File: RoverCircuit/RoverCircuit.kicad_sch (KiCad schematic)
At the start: 57 parts, among them J10 JST_5Pin_P2.54_H, J11_Sample_IR_Diode1 JST_2Pin_P2.54_V, J12_Satellite_IR_Diode1 JST_2Pin_P2.54_V, J13_Laser1 JST_2Pin_P2.54_V, J14_QRD_Board1 JST_5Pin_P2.54_V, J1_Servo1 JST_3Pin_P2.54_V, J2_Left_Wheel1 JST_4Pin_P2.54_V, J3_Right_Wheel1 JST_4Pin_P2.54_V, J4 JST_10Pin_P2.54_V, J5 JST_10Pin_P2.54_V, J6_Left_Sharp1 JST_3Pin_P2.54_V, J7_Right_Sharp1 JST_3Pin_P2.54_V, J8_Front_Sharp1 JST_3Pin_P2.54_V, J9_5v_Regulator1 JST_3Pin_P2.54_V, M1 Motor_Servo, M2 Left_Wheel, M3 Right_Wheel, Q1 PMOS, Q2 NMOS, Q3 QRD1114, Q4 QRD1114, Q5 QRD1114, Q6 NMOS, SW1 SW_SPST, U1 PIC24F16KA301, U2 LM1117T-3.3, U3 LM324

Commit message: Added low pass filters on every analog input
Used R=150, C=0.1uF to attenuate frequencies above the frequency of how fast the AD converter will read each signal.
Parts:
- removed SW1: SW_SPST, symbol Switch:SW_SPST
- added C10, C11, C12, C13, C14, C6, C7, C8, C9: 0.1uF, symbol Device:C
- added C3, C4, C5: 100uF, symbol Device:C_Polarized
- added J15_Ball_QRD1: JST_3Pin_P2.54_V, Connector_JST:JST_EH_B3B-EH-A_1x03_P2.50mm_Vertical, symbol Connector_Generic:Conn_01x03
- added Q7: QRD1114, Diode_THT:Diode_Bridge_DIP-4_W5.08mm_P2.54mm, symbol Custom_Symbol_Library:_1
- added R15: 10kΩ, Resistor_THT:R_Axial_DIN0207_L6.3mm_D2.5mm_P10.16mm_Horizontal, symbol Device:R
- added R16, R17, R18, R19, R20, R21, R22, R23, R24: 150Ω, symbol Device:R
- added R5: 330Ω, Resistor_THT:R_Axial_DIN0207_L6.3mm_D2.5mm_P10.16mm_Horizontal, symbol Device:R
- U1: footprint (none) -> Custom_Library:PIC_board
- U2: footprint Package_TO_SOT_THT:TO-220-3_Horizontal_TabDown -> Package_TO_SOT_THT:TO-220-3_Vertical
- renumbered J12_Satellite_IR_Diode1 to J12_Sat_Diode1
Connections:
- net 12v_Rail: now also Battery1.1 (Pin_1), C3.1
- net 3.3v_Rail: now also R15.2, R5.1
- net 5v_Rail: now also C4.1, C5.1; no longer J1_Servo1.1 (Pin_1), M1.1 (PWM)
- net Ball_Color_QRD_Input: now also C8.1, R18.2
- net Debug_LED_1: now also D1.2 (A)
- net Debug_LED_2: now also D2.2 (A)
- net Front_Sharp_Input: now also C14.1, R24.2; no longer J8_Front_Sharp1.1 (Pin_1), S3. (GND)
- net GND: now also C10.2, C11.2, C12.2, C13.2, C14.2, C3.2, C4.2, C5.2, C6.2, C7.2, C8.2, C9.2, J15_Ball_QRD1.1 (Pin_1), Q7.2 (GND), Q7.4 (GND)
- net Left_Of_Line_QRD_Input: now also C9.1, R19.2; no longer J10.5 (Pin_5), J14_QRD_Board1.5 (Pin_5), Q5.1 (Out), R11.1
- net Left_Sharp_Input: now also C12.1, R22.2; no longer J6_Left_Sharp1.1 (Pin_1), S1. (GND)
- net On_Line_QRD_Input: now also C10.1, R20.2; no longer J10.4 (Pin_4), J14_QRD_Board1.4 (Pin_4), Q4.1 (Out), R12.1
- net Right_Of_Line_QRD_Input: now also C11.1, R21.2; no longer J10.3 (Pin_3), J14_QRD_Board1.3 (Pin_3), Q3.1 (Out), R13.1
- net Right_Sharp_Input: now also C13.1, R23.2; no longer J7_Right_Sharp1.1 (Pin_1), S2. (GND)
- net Sample_Collection_IR_Input: now also C7.1, R17.2; no longer C1.2, R6.2, U3.1
- net Satellite_IR_Input: now also C6.1, R16.2; no longer C2.2, R7.2, U3.7
- net at Q1.1 (D), R1.1: now also J1_Servo1.1 (Pin_1), M1.1 (PWM)
- new net: J15_Ball_QRD1.3 (Pin_3), Q7.3 (Vin), R5.2
- new net Ball_Color_QRD_Output: J15_Ball_QRD1.2 (Pin_2), Q7.1 (Out), R15.1, R18.1
- new net Front_Sharp_Output: J8_Front_Sharp1.1 (Pin_1), R24.1, S3. (GND)
- new net Left_Of_Line_QRD_Output: J10.5 (Pin_5), J14_QRD_Board1.5 (Pin_5), Q5.1 (Out), R11.1, R19.1
- new net Left_Sharp_Output: J6_Left_Sharp1.1 (Pin_1), R22.1, S1. (GND)
- new net On_Line_QRD_Output: J10.4 (Pin_4), J14_QRD_Board1.4 (Pin_4), Q4.1 (Out), R12.1, R20.1
- new net Right_Of_Line_QRD_Output: J10.3 (Pin_3), J14_QRD_Board1.3 (Pin_3), Q3.1 (Out), R13.1, R21.1
- new net Right_Sharp_Output: J7_Right_Sharp1.1 (Pin_1), R23.1, S2. (GND)
- new net Sample_Collection_IR_Output: C1.2, R17.1, R6.2, U3.1
- new net Satellite_IR_Output: C2.2, R16.1, R7.2, U3.7
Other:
- note added: "Signal Conditioning"
- moved on the sheet: Battery1, J10, J13_Laser1, J14_QRD_Board1, J1_Servo1, J9_5v_Regulator1, LD1, M1, Q1, Q2, Q3, Q4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

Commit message: Updated title block
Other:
- company: (none) -> <INSERT NAME HERE> Rihard Bulloch, Kyle Chandler, Dane Baker, Spencer McHenry
- title: (none) -> ME 330: Mars Mini Rover
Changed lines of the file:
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@@
 	(generator_version "9.0")
 	(paper "A4")
+	(title_block
+		(title "ME 330: Mars Mini Rover")
+		(date "2026-10-26")
+		(company "<INSERT NAME HERE> Rihard Bulloch, Kyle Chandler, Dane Baker, Spencer McHenry")
+	)
 	(rectangle
 		(start 201.93 71.12)

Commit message: Added signal conditioning and reorganized the PCB
Also added bulk capacitors on each power rail
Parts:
- removed C5: 100uF, symbol Device:C_Polarized
- added C15: 100uF, Capacitor_THT:CP_Radial_D7.5mm_P2.50mm, symbol Device:C_Polarized
- C10, C11, C12, C13, C14, C6, C7, C8, C9: footprint (none) -> Capacitor_THT:C_Disc_D3.4mm_W2.1mm_P2.50mm
- C3, C4: footprint (none) -> Capacitor_THT:CP_Radial_D7.5mm_P2.50mm
- R16, R17, R18, R19, R20, R21, R22, R23, R24: footprint (none) -> Resistor_THT:R_Axial_DIN0207_L6.3mm_D2.5mm_P10.16mm_Horizontal
- R3, R4: value 330 -> 330Ω
- U1: footprint Custom_Library:PIC_board -> (none)
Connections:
- net 3.3v_Rail: now also C15.1
- net GND: now also C15.2
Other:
- moved on the sheet: U2

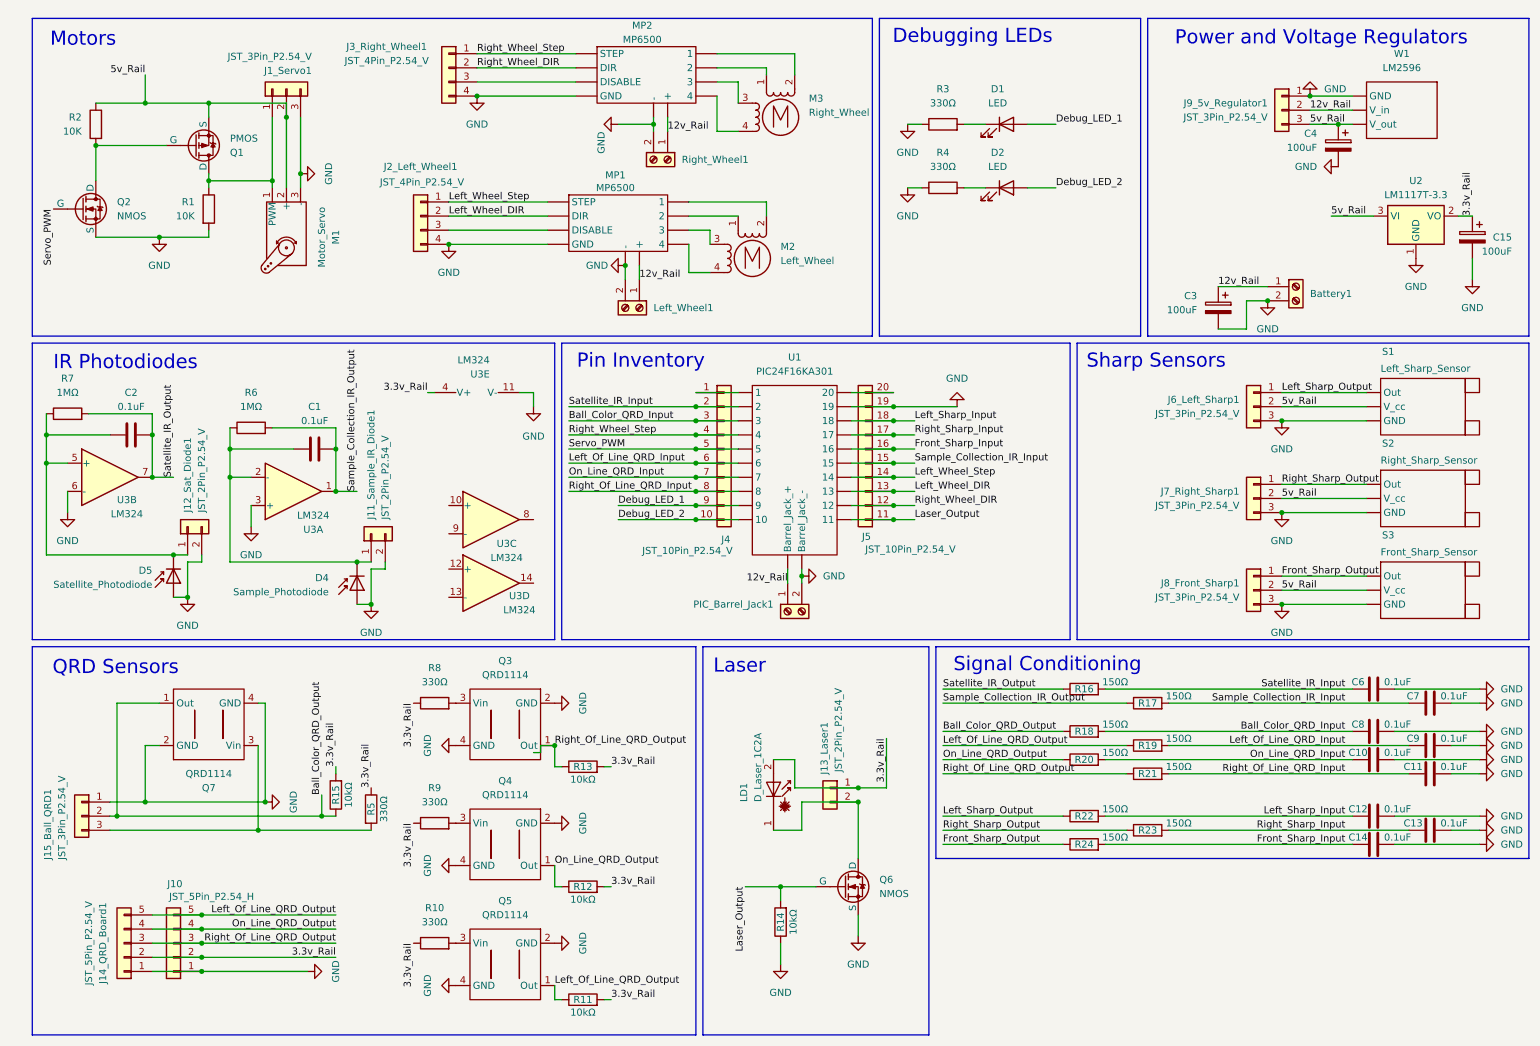
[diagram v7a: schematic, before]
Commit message: Finalized circuit diagram, functional line following
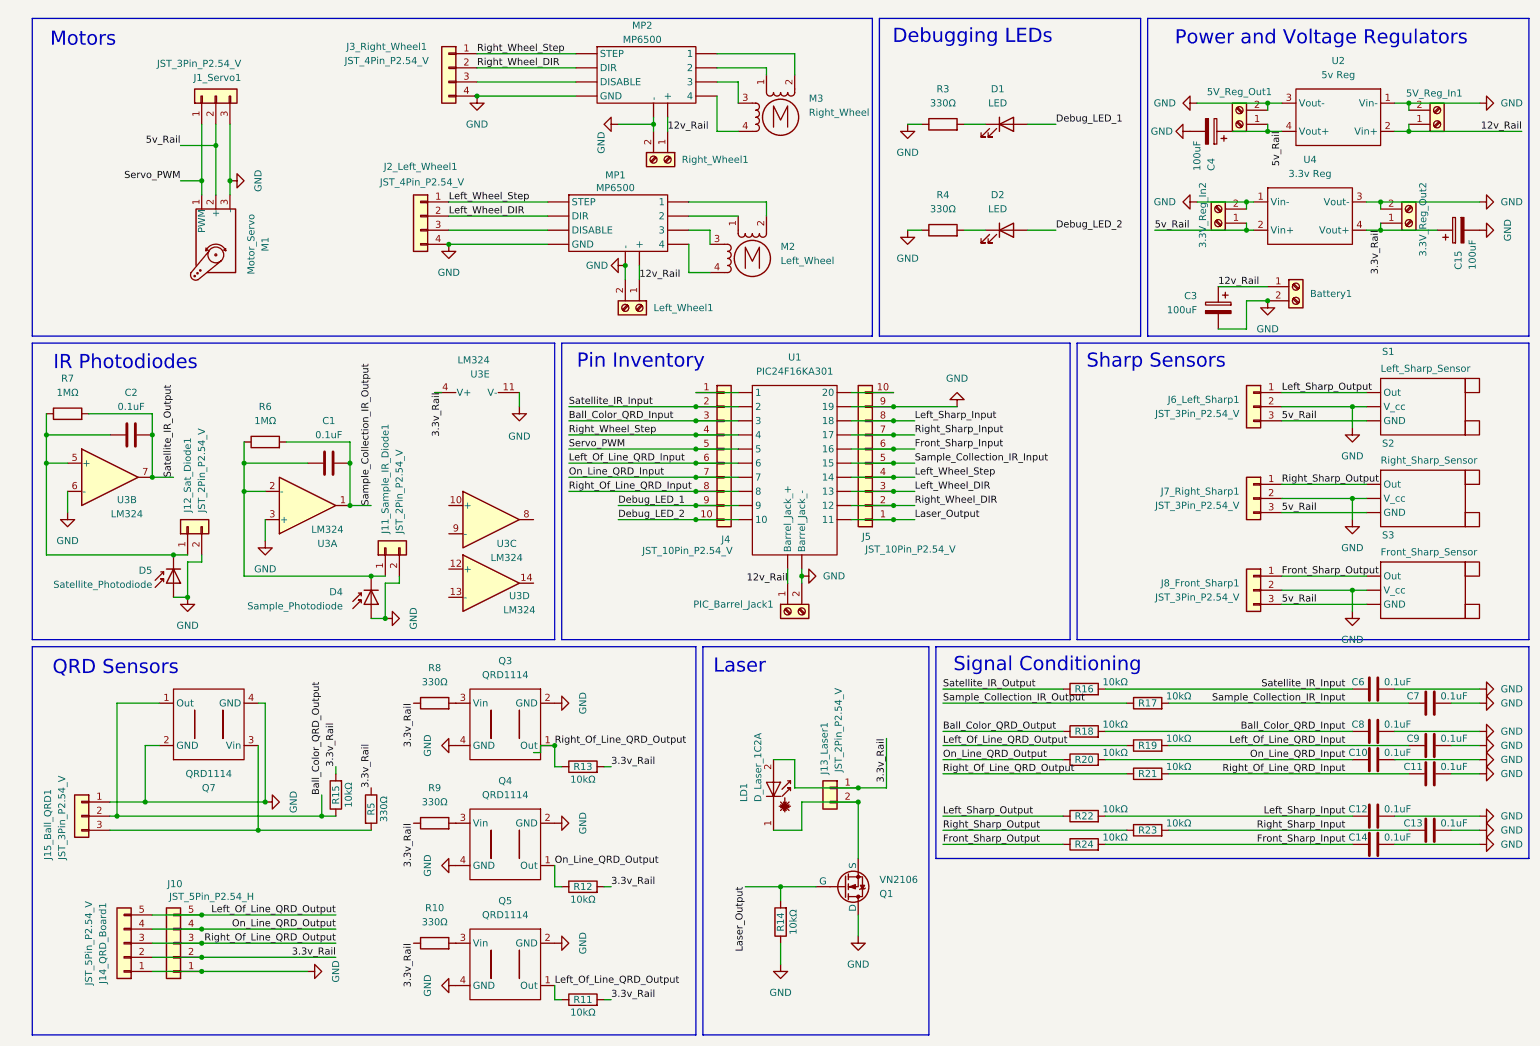
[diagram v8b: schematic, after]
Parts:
- removed J9_5v_Regulator1: JST_3Pin_P2.54_V, Connector_JST:JST_EH_B3B-EH-A_1x03_P2.50mm_Vertical, symbol Connector_Generic:Conn_01x03
- removed Q1: PMOS, Package_TO_SOT_THT:TO-92, symbol Simulation_SPICE:PMOS
- removed Q2: NMOS, Package_TO_SOT_THT:TO-92, symbol Simulation_SPICE:NMOS
- removed R1, R2: 10K, Resistor_THT:R_Axial_DIN0207_L6.3mm_D2.5mm_P10.16mm_Horizontal, symbol Device:R
- removed U2: LM1117T-3.3, Package_TO_SOT_THT:TO-220-3_Vertical, symbol Regulator_Linear:LM1117T-3.3
- removed W1: LM2596, symbol Custom_Symbol_Library:LM2596 - 5v Buck Converter
- added 3.3V_Reg_In2, 3.3V_Reg_Out2, 5V_Reg_In1, 5V_Reg_Out1: Battery_Terminal, Custom_Library:screw_terminal, symbol Connector:Screw_Terminal_01x02
- added U2: 5v Reg, symbol Custom_Symbol_Library:Variable_Voltage_Regulator
- added U4: 3.3v Reg, symbol Custom_Symbol_Library:Variable_Voltage_Regulator
- Q1: renamed from Q6; value NMOS -> VN2106; footprint Package_TO_SOT_THT:TO-92 -> Package_TO_SOT_THT:TO-92S
- R16, R17, R18, R19, R20, R21, R22, R23, R24: value 150Ω -> 10kΩ
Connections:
- net 12v_Rail: now also 5V_Reg_In1.1 (Pin_1), U2.2 (Vin+)
- net 3.3v_Rail: now also 3.3V_Reg_Out2.1 (Pin_1), U4.4 (Vout+)
- net 5v_Rail: now also J6_Left_Sharp1.3 (Pin_3), J7_Right_Sharp1.3 (Pin_3), J8_Front_Sharp1.3 (Pin_3), 3.3V_Reg_In2.1 (Pin_1), 5V_Reg_Out1.1 (Pin_1), U2.4 (Vout+), U4.2 (Vin+); no longer J6_Left_Sharp1.2 (Pin_2), J7_Right_Sharp1.2 (Pin_2), J8_Front_Sharp1.2 (Pin_2)
- net Front_Sharp_Input: now also J5.6 (Pin_6); no longer J5.16 (Pin_6)
- net GND: now also J5.9 (Pin_9), J6_Left_Sharp1.2 (Pin_2), J7_Right_Sharp1.2 (Pin_2), J8_Front_Sharp1.2 (Pin_2), Q1.1 (D), 3.3V_Reg_In2.2 (Pin_2), 3.3V_Reg_Out2.2 (Pin_2), 5V_Reg_In1.2 (Pin_2), 5V_Reg_Out1.2 (Pin_2), U2.1 (Vin-), U2.3 (Vout-), U4.1 (Vin-), U4.3 (Vout-); no longer J5.19 (Pin_9), J6_Left_Sharp1.3 (Pin_3), J7_Right_Sharp1.3 (Pin_3), J8_Front_Sharp1.3 (Pin_3), Q1.3 (S)
- net Laser_Output: now also J5.1 (Pin_1); no longer J5.11 (Pin_1)
- net Left_Sharp_Input: now also J5.8 (Pin_8); no longer J5.18 (Pin_8)
- net Left_Wheel_DIR: now also J5.3 (Pin_3); no longer J5.13 (Pin_3)
- net Left_Wheel_Step: now also J5.4 (Pin_4); no longer J5.14 (Pin_4)
- net Right_Sharp_Input: now also J5.7 (Pin_7); no longer J5.17 (Pin_7)
- net Right_Wheel_DIR: now also J5.2 (Pin_2); no longer J5.12 (Pin_2)
- net Sample_Collection_IR_Input: now also J5.5 (Pin_5); no longer J5.15 (Pin_5)
- net Servo_PWM: now also J1_Servo1.1 (Pin_1), M1.1 (PWM)
- net at J13_Laser1.2 (Pin_2), LD1.1 (K): now also Q1.3 (S); no longer Q1.1 (D)
- new net: J5.10 (Pin_10), U1. (11)
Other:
- company: <INSERT NAME HERE> Rihard Bulloch, Kyle Chandler, Dane Baker, Spencer McHenry -> <INSERT NAME HERE> Richard Bulloch, Kyle Chandler, Dane Baker, Spencer McHenry
- moved on the sheet: C1, C15, D2, D4, J11_Sample_IR_Diode1, J1_Servo1, M1, R4, R6, U3A
